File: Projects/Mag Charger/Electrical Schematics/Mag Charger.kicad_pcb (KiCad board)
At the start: 2 copper layers, 26 x 27.9 mm, 11 parts, among them P1 USB_C_Plug_USB2.0, U1 AP2112K-3.3

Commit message: Added ESD to mag charger schematic
Also worked on preliminary PCB layout.
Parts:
- removed R1: 5.1k, Resistor_SMD:R_0603_1608Metric
- removed U1: AP2112K-3.3, Package_TO_SOT_SMD:SOT-23-5
- added D1: SMF20A, Diode_SMD:D_SMF, F.Cu at (111.8, 138.1)
- added D2: ESD862DBZR, Package_TO_SOT_SMD:SOT-23_Handsoldering, F.Cu at (108.3, 138.1)
- added J1: Conn_01x08, Mag Charger:Mag Connector, F.Cu at (108.3, 148.0)
- C1, C2: value 10uF -> C; footprint Capacitor_SMD:C_0805_2012Metric -> Capacitor_SMD:C_1206_3216Metric_Pad1.33x1.80mm_HandSolder
- P1: value USB_C_Plug_USB2.0 -> USB_C_Plug
- moved C1 22.6 mm to (120.0, 137.4), turned to 90 degrees
- moved C2 3.16 mm to (96.8, 137.5), turned to 90 degrees
- turned H1 to 90 degrees
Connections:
- C2 pad 1: +3V3 -> VBUS
- P1 pad A10: (no net) -> unconnected-(P1-RX2--PadA10)
- P1 pad A11: (no net) -> unconnected-(P1-RX2+-PadA11)
- P1 pad A2: (no net) -> /USB_TX1+
- P1 pad A3: (no net) -> /USB_TX1-
- P1 pad A5: Net-(P1-PadA5) -> /USB_CC
- P1 pad A6: (no net) -> /USB_DP
- P1 pad A7: (no net) -> /USB_DN
- P1 pad A8: (no net) -> unconnected-(P1-SBU1-PadA8)
- P1 pad B10: (no net) -> /USB_RX1-
- P1 pad B11: (no net) -> /USB_RX1+
- P1 pad B2: (no net) -> unconnected-(P1-TX2+-PadB2)
- P1 pad B3: (no net) -> unconnected-(P1-TX2--PadB3)
- P1 pad B5: (no net) -> /USB_VCONN
- P1 pad B8: (no net) -> unconnected-(P1-SBU2-PadB8)
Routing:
- net GND: track 0.00 -> 26.3 mm, vias 8 -> 12
- net /USB_VCONN: track 0.00 -> 26.2 mm, vias 0 -> 1
- net /USB_CC: track 0.00 -> 24.2 mm
- net /USB_DP: track 0.00 -> 24.0 mm, vias 0 -> 1
- net /USB_DN: track 0.00 -> 24.0 mm, vias 0 -> 1
- net VBUS: track 0.00 -> 4.86 mm, vias 0 -> 2
- added copper zone on B.Cu, net GND
- added copper zone on F.Cu, net VBUS
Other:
- board size 26 x 27.9 mm -> 26 x 25.7 mm

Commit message: Finalized I2C Card
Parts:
- D1: value SMF20A -> SMBJ51ACT-ND
- P1: value USB_C_Plug -> USB_C_Plug_USB2.0
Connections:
- P1 pad A10: unconnected-(P1-RX2--PadA10) -> (no net)
- P1 pad A11: unconnected-(P1-RX2+-PadA11) -> (no net)
- P1 pad A2: /USB_TX1+ -> (no net)
- P1 pad A3: /USB_TX1- -> (no net)
- P1 pad A8: unconnected-(P1-SBU1-PadA8) -> (no net)
- P1 pad B10: /USB_RX1- -> (no net)
- P1 pad B11: /USB_RX1+ -> (no net)
- P1 pad B2: unconnected-(P1-TX2+-PadB2) -> (no net)
- P1 pad B3: unconnected-(P1-TX2--PadB3) -> (no net)
- P1 pad B8: unconnected-(P1-SBU2-PadB8) -> (no net)
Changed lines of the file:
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@@
 	(net 3 "VBUS")
 	(net 4 "/USB_DP")
-	(net 5 "/USB_TX1+")
-	(net 6 "/USB_TX1-")
-	(net 7 "unconnected-(P1-SBU1-PadA8)")
-	(net 8 "unconnected-(P1-RX2--PadA10)")
-	(net 9 "unconnected-(P1-RX2+-PadA11)")
-	(net 10 "unconnected-(P1-TX2+-PadB2)")
-	(net 11 "unconnected-(P1-TX2--PadB3)")
-	(net 12 "unconnected-(P1-SBU2-PadB8)")
-	(net 13 "/USB_RX1-")
-	(net 14 "/USB_RX1+")
-	(net 15 "/USB_CC")
-	(net 16 "/USB_VCONN")
+	(net 5 "/USB_CC")
+	(net 6 "/USB_VCONN")
 	(footprint "MountingHole:MountingHole_2.2mm_M2"
 		(layer "F.Cu")
@@
 			)
 		)
-		(property "Value" "USB_C_Plug"
+		(property "Value" "USB_C_Plug_USB2.0"
 			(at 0 -1.96 0)
 			(layer "F.Fab")
@@
 			)
 		)
-		(property "Description" "USB Type-C Plug connector"
+		(property "Description" ""
 			(at 0 0 0)
 			(layer "F.Fab")
@@
 			)
 		)
+		(property ki_fp_filters "USB*C*Plug*")
+		(sheetname "/")
+		(sheetfile "Mag Charger.kicad_sch")
 		(attr smd)
 		(fp_line
@@
 			(size 0.38 1)
 			(layers "F.Cu" "F.Mask" "F.Paste")
-			(net 5 "/USB_TX1+")
-			(pinfunction "TX1+")
-			(pintype "bidirectional")
 		)
 		(pad "A3" smd rect
@@
 			(size 0.38 1)
 			(layers "F.Cu" "F.Mask" "F.Paste")
-			(net 6 "/USB_TX1-")
-			(pinfunction "TX1-")
-			(pintype "bidirectional")
 		)
 		(pad "A4" smd rect
@@
 			(size 0.38 1)
 			(layers "F.Cu" "F.Mask" "F.Paste")
-			(net 15 "/USB_CC")
+			(net 5 "/USB_CC")
 			(pinfunction "CC")
 			(pintype "bidirectional")
@@
 			(size 0.38 1)
 			(layers "F.Cu" "F.Mask" "F.Paste")
-			(net 7 "unconnected-(P1-SBU1-PadA8)")
-			(pinfunction "SBU1")
-			(pintype "bidirectional+no_connect")
 		)
 		(pad "A9" smd rect
@@
 			(size 0.38 1)
 			(layers "F.Cu" "F.Mask" "F.Paste")
-			(net 8 "unconnected-(P1-RX2--PadA10)")
-			(pinfunction "RX2-")
-			(pintype "bidirectional+no_connect")
 		)
 		(pad "A11" smd rect
@@
 			(size 0.38 1)
 			(layers "F.Cu" "F.Mask" "F.Paste")
-			(net 9 "unconnected-(P1-RX2+-PadA11)")
-			(pinfunction "RX2+")
-			(pintype "bidirectional+no_connect")
 		)
 		(pad "A12" smd rect
@@
 			(size 0.38 1)
 			(layers "B.Cu" "B.Mask" "B.Paste")
-			(net 10 "unconnected-(P1-TX2+-PadB2)")
-			(pinfunction "TX2+")
-			(pintype "bidirectional+no_connect")
 		)
 		(pad "B3" smd rect
@@
 			(size 0.38 1)
 			(layers "B.Cu" "B.Mask" "B.Paste")
-			(net 11 "unconnected-(P1-TX2--PadB3)")
-			(pinfunction "TX2-")
-			(pintype "bidirectional+no_connect")
 		)
 		(pad "B4" smd rect
@@
 			(size 0.38 1)
 			(layers "B.Cu" "B.Mask" "B.Paste")
-			(net 16 "/USB_VCONN")
+			(net 6 "/USB_VCONN")
 			(pinfunction "VCONN")
-			(pintype "bidirectional+no_connect")
+			(pintype "bidirectional")
 		)
 		(pad "B8" smd rect
@@
 			(size 0.38 1)
 			(layers "B.Cu" "B.Mask" "B.Paste")
-			(net 12 "unconnected-(P1-SBU2-PadB8)")
-			(pinfunction "SBU2")
-			(pintype "bidirectional+no_connect")
 		)
 		(pad "B9" smd rect
@@
 			(size 0.38 1)
 			(layers "B.Cu" "B.Mask" "B.Paste")
-			(net 13 "/USB_RX1-")
-			(pinfunction "RX1-")
-			(pintype "bidirectional")
 		)
 		(pad "B11" smd rect
@@
 			(size 0.38 1)
 			(layers "B.Cu" "B.Mask" "B.Paste")
-			(net 14 "/USB_RX1+")
-			(pinfunction "RX1+")
-			(pintype "bidirectional")
 		)
 		(pad "B12" smd rect
@@
 			)
 		)
-		(property "Value" "SMF20A"
+		(property "Value" "SMBJ51ACT-ND"
 			(at 0 2 90)
 			(layer "F.Fab")
@@
 			)
 		)
-		(property "Datasheet" "https://www.vishay.com/doc?85881"
+		(property "Datasheet" "https://www.diodes.com/assets/Datasheets/ds19002.pdf"
 			(at 0 0 90)
 			(unlocked yes)
@@
 			)
 		)
-		(property "Description" "200W unidirectional Transil Transient Voltage Suppressor, 20Vrwm, SMF"
+		(property "Description" "TVS DIODE 51VWM 82.4VC DO214AA"
 			(at 0 0 90)
 			(unlocked yes)
@@
 			(remove_unused_layers no)
 			(roundrect_rratio 0.2083333333)
-			(net 15 "/USB_CC")
+			(net 5 "/USB_CC")
 			(pinfunction "Pin_3")
 			(pintype "passive")
@@
 			(remove_unused_layers no)
 			(roundrect_rratio 0.2083333333)
-			(net 16 "/USB_VCONN")
+			(net 6 "/USB_VCONN")
 			(pinfunction "Pin_6")
 			(pintype "passive")
@@
 		(width 0.2)
 		(layer "F.Cu")
-		(net 15)
+		(net 5)
 	)
 	(segment
@@
 		(width 0.2)
 		(layer "F.Cu")
-		(net 15)
+		(net 5)
 	)
 	(segment
@@
 		(width 0.2)
 		(layer "F.Cu")
-		(net 15)
+		(net 5)
 	)
 	(segment
@@
 		(width 0.2)
 		(layer "F.Cu")
-		(net 16)
+		(net 6)
 	)
 	(segment
@@
 		(width 0.2)
 		(layer "F.Cu")
-		(net 16)
+		(net 6)
 	)
 	(segment
@@
 		(width 0.2)
 		(layer "F.Cu")
-		(net 16)
+		(net 6)
 	)
 	(segment
@@
 		(width 0.2)
 		(layer "F.Cu")
-		(net 16)
+		(net 6)
 	)
 	(via
@@
 		(drill 0.3)
 		(layers "F.Cu" "B.Cu")
-		(net 16)
+		(net 6)
 	)
 	(segment
@@
 		(width 0.2)
 		(layer "B.Cu")
-		(net 16)
+		(net 6)
 	)
 	(segment
@@
 		(width 0.2)
 		(layer "B.Cu")
-		(net 16)
+		(net 6)
 	)
 	(zone

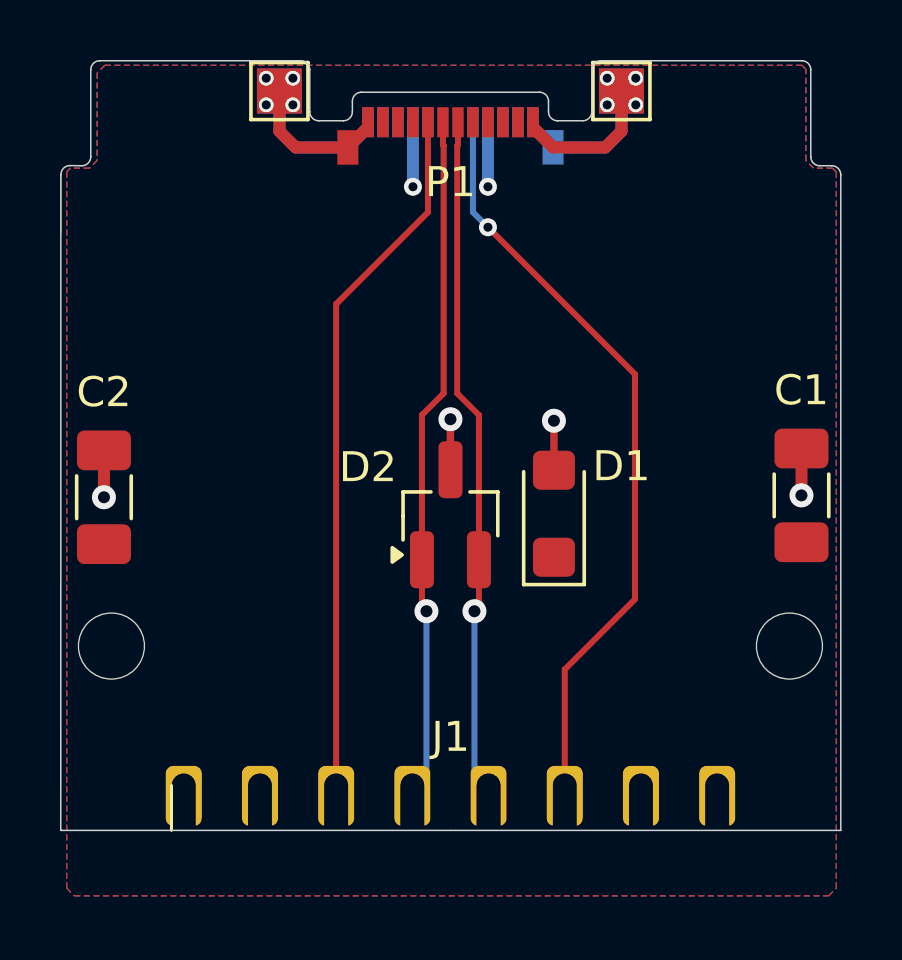
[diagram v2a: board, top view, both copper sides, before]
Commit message: Fixed DRC for card
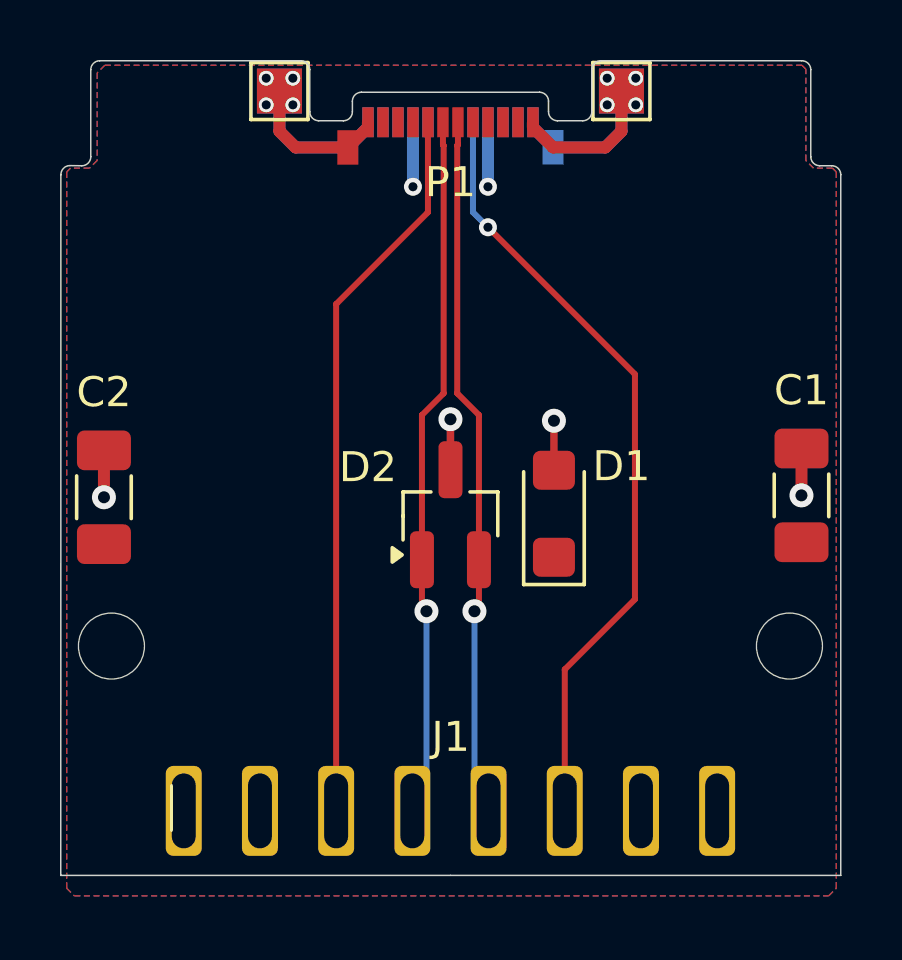
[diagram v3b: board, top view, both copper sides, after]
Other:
- board size 26 x 25.7 mm -> 26 x 27.2 mm
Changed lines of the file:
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@@
 			(layer "F.SilkS")
 		)
-		(fp_rect
-			(start -14.85 0.65)
-			(end 14.85 4.65)
-			(stroke
-				(width 0.1)
+		(fp_line
+			(start 0 2.15)
+			(end -12.99 2.15)
+			(stroke
+				(width 0.05)
 				(type default)
 			)
-			(fill no)
-			(layer "Dwgs.User")
-		)
-		(fp_line
-			(start 0 0.65)
-			(end -12.99 0.65)
-			(stroke
-				(width 0.05)
-				(type default)
-			)
 			(layer "Edge.Cuts")
 		)
 		(fp_line
-			(start 0 0.65)
-			(end 13.01 0.65)
+			(start 0 2.15)
+			(end 13.01 2.15)
 			(stroke
 				(width 0.05)
@@
 		(pad "1" thru_hole roundrect
 			(at -8.89 0)
-			(size 1.2 2)
-			(drill oval 0.8 2.5
-				(offset 0 -0.5)
-			)
+			(size 1.2 3)
+			(drill oval 0.8 2.5)
 			(layers "*.Cu" "*.Mask")
 			(remove_unused_layers no)
@@
 		(pad "2" thru_hole roundrect
 			(at -6.35 0)
-			(size 1.2 2)
-			(drill oval 0.8 2.5
-				(offset 0 -0.5)
-			)
+			(size 1.2 3)
+			(drill oval 0.8 2.5)
 			(layers "*.Cu" "*.Mask")
 			(remove_unused_layers no)
@@
 		(pad "3" thru_hole roundrect
 			(at -3.81 0)
-			(size 1.2 2)
-			(drill oval 0.8 2.5
-				(offset 0 -0.5)
-			)
+			(size 1.2 3)
+			(drill oval 0.8 2.5)
 			(layers "*.Cu" "*.Mask")
 			(remove_unused_layers no)
@@
 		(pad "4" thru_hole roundrect
 			(at -1.27 0)
-			(size 1.2 2)
-			(drill oval 0.8 2.5
-				(offset 0 -0.5)
-			)
+			(size 1.2 3)
+			(drill oval 0.8 2.5)
 			(layers "*.Cu" "*.Mask")
 			(remove_unused_layers no)
@@
 		(pad "5" thru_hole roundrect
 			(at 1.27 0)
-			(size 1.2 2)
-			(drill oval 0.8 2.5
-				(offset 0 -0.5)
-			)
+			(size 1.2 3)
+			(drill oval 0.8 2.5)
 			(layers "*.Cu" "*.Mask")
 			(remove_unused_layers no)
@@
 		(pad "6" thru_hole roundrect
 			(at 3.81 0)
-			(size 1.2 2)
-			(drill oval 0.8 2.5
-				(offset 0 -0.5)
-			)
+			(size 1.2 3)
+			(drill oval 0.8 2.5)
 			(layers "*.Cu" "*.Mask")
 			(remove_unused_layers no)
@@
 		(pad "7" thru_hole roundrect
 			(at 6.35 0)
-			(size 1.2 2)
-			(drill oval 0.8 2.5
-				(offset 0 -0.5)
-			)
+			(size 1.2 3)
+			(drill oval 0.8 2.5)
 			(layers "*.Cu" "*.Mask")
 			(remove_unused_layers no)
@@
 		(pad "8" thru_hole roundrect
 			(at 8.89 0)
-			(size 1.2 2)
-			(drill oval 0.8 2.5
-				(offset 0 -0.5)
-			)
+			(size 1.2 3)
+			(drill oval 0.8 2.5)
 			(layers "*.Cu" "*.Mask")
 			(remove_unused_layers no)
@@
 	)
 	(gr_line
-		(start 121.31105 148.605)
+		(start 121.31 150.105)
 		(end 121.31105 126.75)
 		(stroke
@@
 	(gr_line
 		(start 95.31585 126.7452)
-		(end 95.31 148.605)
-		(stroke
-			(width 0.05)
+		(end 95.31 150.105)
+		(stroke
+			(width 0.05)

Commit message: Updated diode models
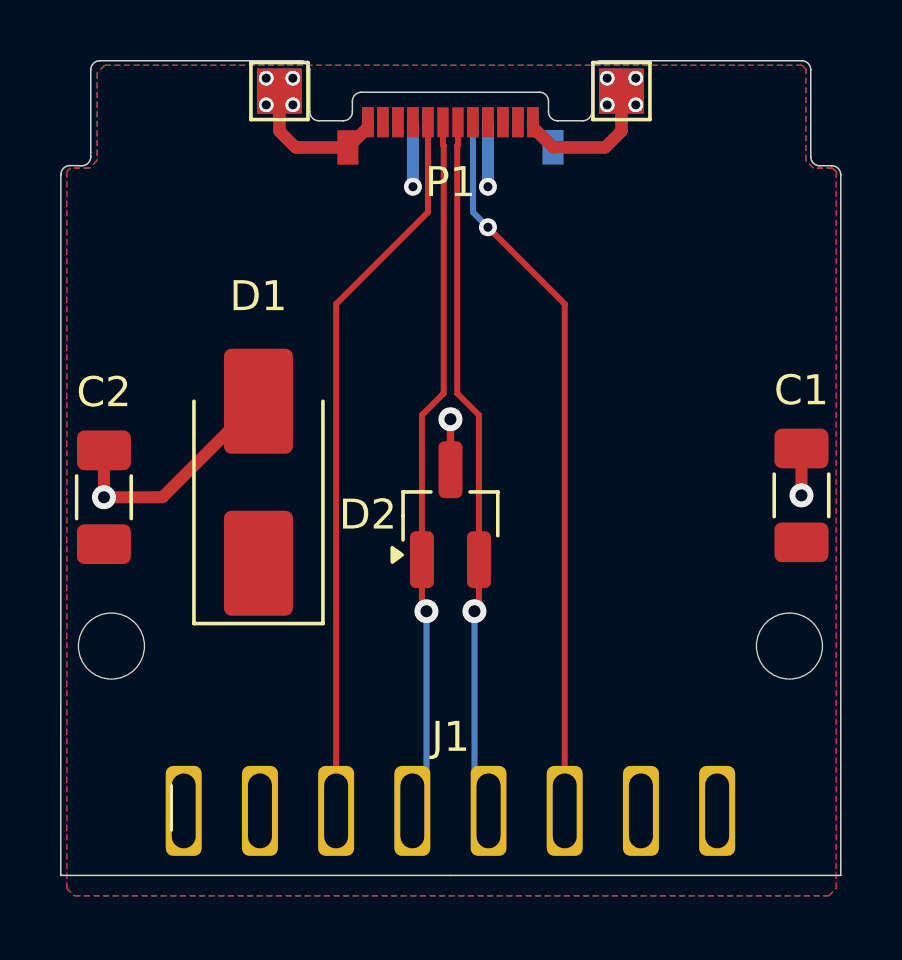
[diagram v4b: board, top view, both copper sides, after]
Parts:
- D1: footprint Diode_SMD:D_SMF -> Diode_SMD:D_SMB_Handsoldering
- moved D1 9.91 mm to (101.9, 137.0)
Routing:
- net GND: track 26.3 -> 31.1 mm, vias 12 -> 11
- net /USB_VCONN: track 26.2 -> 24.2 mm
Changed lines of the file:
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@@
 		)
 	)
-	(footprint "Diode_SMD:D_SMF"
-		(layer "F.Cu")
-		(at 111.75 138.05 90)
-		(descr "Diode SMF (DO-219AB), http://www.vishay.com/docs/95572/smf_do-219ab.pdf")
-		(tags "Diode SMF (DO-214AB)")
+	(footprint "Diode_SMD:D_SMB_Handsoldering"
+		(layer "F.Cu")
+		(at 101.9 137 90)
+		(descr "Diode SMB (DO-214AA) Handsoldering")
+		(tags "Diode SMB (DO-214AA) Handsoldering")
 		(property "Reference" "D1"
-			(at 1.582 2.25 180)
+			(at 6.2 0 180)
 			(layer "F.SilkS")
 			(effects
@@
 		)
 		(property "Value" "SMBJ51ACT-ND"
-			(at 0 2 90)
+			(at 0 3 90)
 			(layer "F.Fab")
 			(effects
@@
 		(attr smd)
 		(fp_line
-			(start -2.36 -1.01)
-			(end 1.4 -1.01)
+			(start -4.71 -2.15)
+			(end 2.7 -2.15)
 			(stroke
 				(width 0.12)
@@
 		)
 		(fp_line
-			(start -2.36 -1.01)
-			(end -2.36 1.01)
+			(start -4.71 -2.15)
+			(end -4.71 2.15)
 			(stroke
 				(width 0.12)
@@
 		)
 		(fp_line
-			(start -2.36 1.01)
-			(end 1.4 1.01)
+			(start -4.71 2.15)
+			(end 2.7 2.15)
 			(stroke
 				(width 0.12)
@@
 		)
 		(fp_line
-			(start 2.35 -1.15)
-			(end 2.35 1.15)
+			(start 4.7 -2.25)
+			(end 4.7 2.25)
 			(stroke
 				(width 0.05)
@@
 		)
 		(fp_line
-			(start -2.35 -1.15)
-			(end 2.35 -1.15)
+			(start -4.7 -2.25)
+			(end 4.7 -2.25)
 			(stroke
 				(width 0.05)
@@
 		)
 		(fp_line
-			(start 2.35 1.15)
-			(end -2.35 1.15)
+			(start 4.7 2.25)
+			(end -4.7 2.25)
 			(stroke
 				(width 0.05)
@@
 		)
 		(fp_line
-			(start -2.35 1.15)
-			(end -2.35 -1.15)
+			(start -4.7 2.25)
+			(end -4.7 -2.25)
 			(stroke
 				(width 0.05)
@@
 		)
 		(fp_line
-			(start 1.4 -0.9)
-			(end -1.4 -0.9)
+			(start 2.3 -2)
+			(end -2.3 -2)
 			(stroke
 				(width 0.1)
@@
 		)
 		(fp_line
-			(start 1.4 -0.9)
-			(end 1.4 0.9)
+			(start 2.3 -2)
+			(end 2.3 2)
 			(stroke
 				(width 0.1)
@@
 		)
 		(fp_line
-			(start -0.3 -0.4)
-			(end -0.3 0.4)
+			(start -0.64944 -0.79908)
+			(end -0.64944 0.80112)
 			(stroke
 				(width 0.1)
@@
 		)
 		(fp_line
-			(start 0.3 0)
-			(end 0.9 0)
+			(start 0.50118 0.00102)
+			(end 1.4994 0.00102)
 			(stroke
 				(width 0.1)
@@
 		)
 		(fp_line
-			(start -0.3 0)
-			(end 0.3 -0.4)
+			(start -0.64944 0.00102)
+			(end 0.50118 -0.79908)
 			(stroke
 				(width 0.1)
@@
 		)
 		(fp_line
-			(start -0.3 0)
-			(end -0.9 0)
+			(start -0.64944 0.00102)
+			(end -1.55114 0.00102)
 			(stroke
 				(width 0.1)
@@
 		)
 		(fp_line
-			(start -0.3 0.00102)
-			(end 0.3 0.4)
+			(start -0.64944 0.00102)
+			(end 0.50118 0.75032)
 			(stroke
 				(width 0.1)
@@
 		)
 		(fp_line
-			(start 0.3 0.4)
-			(end 0.3 -0.4)
+			(start 0.50118 0.75032)
+			(end 0.50118 -0.79908)
 			(stroke
 				(width 0.1)
@@
 		)
 		(fp_line
-			(start 1.4 0.9)
-			(end -1.4 0.9)
+			(start 2.3 2)
+			(end -2.3 2)
 			(stroke
 				(width 0.1)
@@
 		)
 		(fp_line
-			(start -1.4 0.9)
-			(end -1.4 -0.9)
+			(start -2.3 2)
+			(end -2.3 -2)
 			(stroke
 				(width 0.1)
@@
 		)
 		(fp_text user "${REFERENCE}"
-			(at 0 -2 90)
+			(at 0 -3 90)
 			(layer "F.Fab")
 			(effects
@@
 		)
 		(pad "1" smd roundrect
-			(at -1.45 0 90)
-			(size 1.3 1.4)
+			(at -2.7 0 90)
+			(size 3.5 2.3)
 			(layers "F.Cu" "F.Mask" "F.Paste")
-			(roundrect_rratio 0.1923076923)
+			(roundrect_rratio 0.1086956522)
 			(net 3 "VBUS")
 			(pinfunction "A1")
@@
 		)
 		(pad "2" smd roundrect
-			(at 1.45 0 90)
-			(size 1.3 1.4)
+			(at 2.7 0 90)
+			(size 3.5 2.3)
 			(layers "F.Cu" "F.Mask" "F.Paste")
-			(roundrect_rratio 0.1923076923)
+			(roundrect_rratio 0.1086956522)
 			(net 1 "GND")
 			(pinfunction "A2")
@@
 		)
 		(embedded_fonts no)
-		(model "${KICAD9_3DMODEL_DIR}/Diode_SMD.3dshapes/D_SMF.step"
+		(model "${KICAD9_3DMODEL_DIR}/Diode_SMD.3dshapes/D_SMB.step"
 			(offset
 				(xyz 0 0 0)
@@
 		(tags "SOT-23")
 		(property "Reference" "D2"
-			(at 1.582 -2.75 180)
+			(at 0 -2.75 180)
 			(layer "F.SilkS")
 			(effects
@@
 		)
 		(fp_text user "${REFERENCE}"
-			(at 0 0 0)
+			(at 0 0 180)
 			(layer "F.Fab")
 			(effects
@@
 	)
 	(segment
+		(start 98.7 137.5)
+		(end 101.9 134.3)
+		(width 0.4)
+		(layer "F.Cu")
+		(net 1)
+	)
+	(segment
 		(start 113.46 125.84)
 		(end 114 125.3)
@@
 	)
 	(segment
-		(start 111.75 134.95)
-		(end 111.75 136.6)
-		(width 0.25)
-		(layer "F.Cu")
-		(net 1)
-	)
-	(segment
 		(start 111.72 125.84)
 		(end 113.46 125.84)
@@
 		(start 111.05 125.17)
 		(end 111.72 125.84)
+		(width 0.4)
+		(layer "F.Cu")
+		(net 1)
+	)
+	(segment
+		(start 96.75 137.5)
+		(end 98.7 137.5)
 		(width 0.4)
 		(layer "F.Cu")
@@
 	)
 	(via
-		(at 111.75 134.95)
-		(size 0.8)
-		(drill 0.4)
-		(layers "F.Cu" "B.Cu")
-		(free yes)
-		(net 1)
-	)
-	(via
 		(at 113.5245 123.5315)
 		(size 0.5)
@@
 	(segment
 		(start 109.55 128.5)
-		(end 114.45 133.4)
+		(end 112.11 131.06)
 		(width 0.2)
 		(layer "F.Cu")
@@
 	)
 	(segment
-		(start 114.45 133.4)
-		(end 114.45 140.9)
-		(width 0.2)
-		(layer "F.Cu")
-		(net 6)
-	)
-	(segment
-		(start 112.11 143.24)
+		(start 112.11 131.06)
 		(end 112.11 147.955)
 		(width 0.2)
 		(layer "F.Cu")
-		(net 6)
-	)
-	(segment
-		(start 114.45 140.9)
-		(end 112.11 143.24)
-		(width 0.2)
-		(layer "F.Cu")
